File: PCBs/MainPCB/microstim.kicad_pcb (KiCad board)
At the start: 2 copper layers, 124.5 x 79.5 mm, 105 parts, among them J1 Conn_02x08_Odd_Even, J2 Conn_Coaxial, J3 Conn_Coaxial, J6 Screw_Terminal_01x02, J7 Conn_Coaxial, J8 Screw_Terminal_01x02, J9 Conn_Coaxial, SW1 SW_Push, U1 Teensy3.5, U10 AD8276, U11 INA826, U12 DG509ACWE, U13 CC3-0512DF-E, U14 ISO7760, U15 ISO7341C, U16 L78L05_SO8, U17 AD5752, U18 AD7321, U19 AD1582, U2 CC3-0512DF-E, U20 OPA197, U21 AD8276, U22 INA826, U23 DG509ACWE, U3 ISO7760, U4 ISO7341C, U5 L78L05_SO8, U6 AD5752, U7 AD7321, U8 AD1582, U9 OPA197

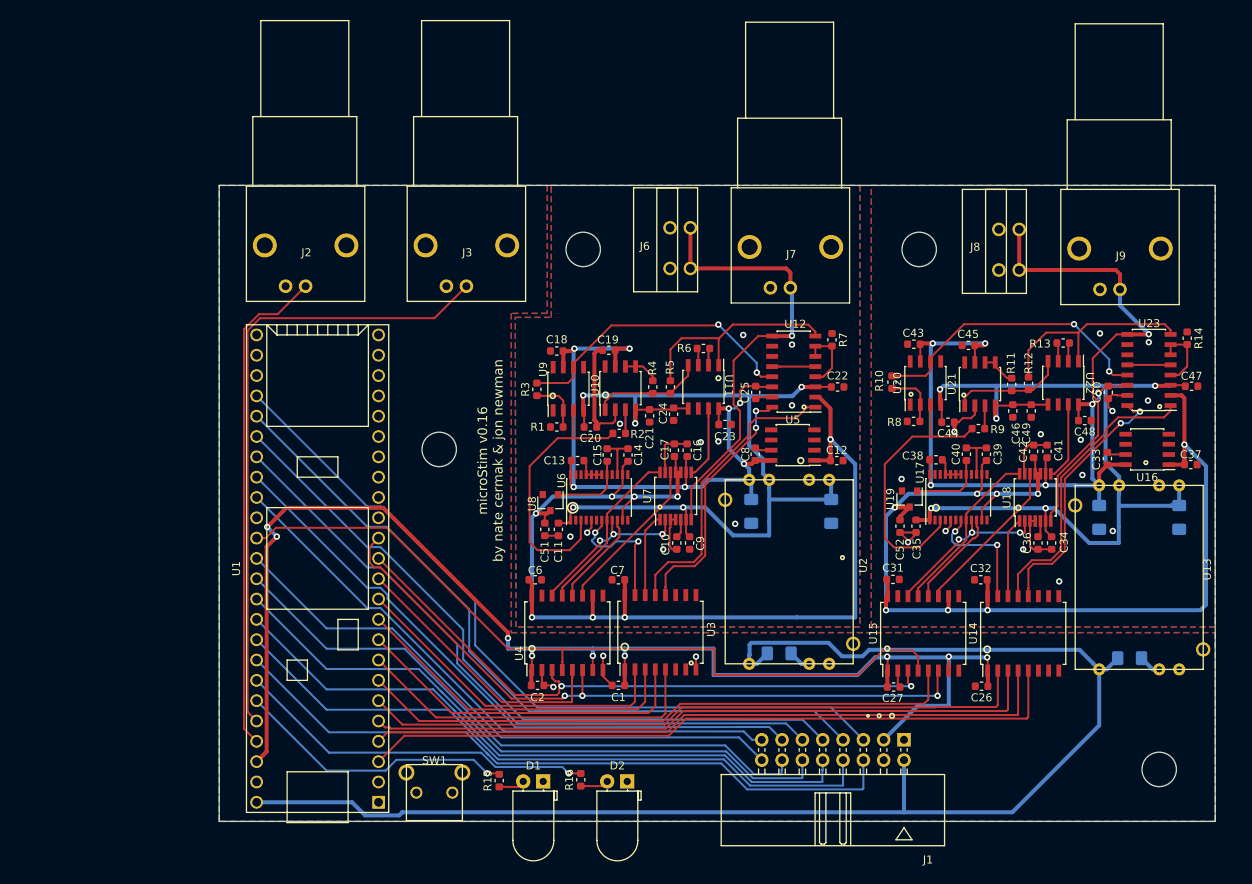
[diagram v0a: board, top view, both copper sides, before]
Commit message: increased board size to 129x79.5 from 124.5x79.5, changed enclosure to something on digikey rather than newark. also added trigger capability to teensy code
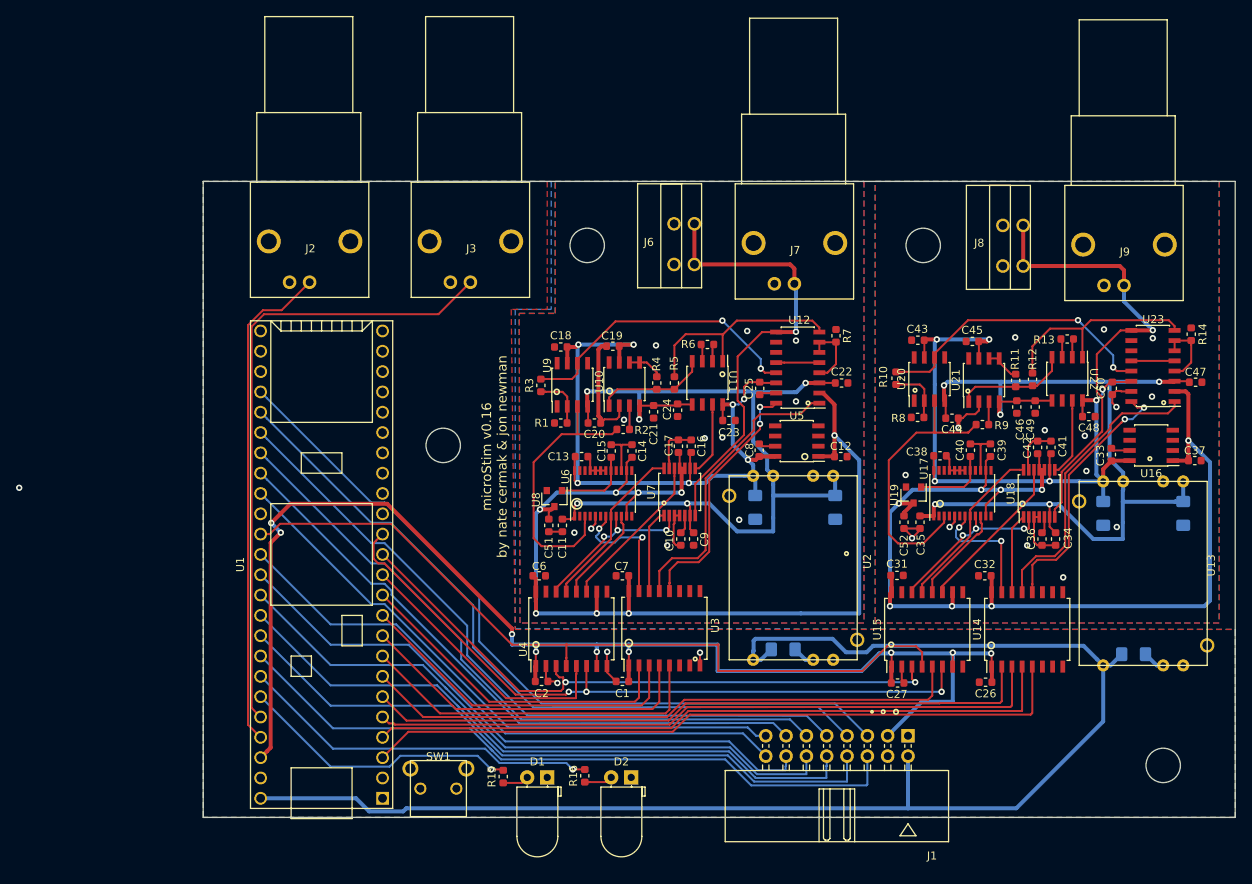
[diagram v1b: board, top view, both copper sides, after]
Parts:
- moved C1 0.71 mm to (132.9, 114.0)
- moved C10 0.71 mm to (140.2, 96.2)
- moved C11 0.71 mm to (125.4, 94.5)
- moved C12 0.71 mm to (160.2, 85.9)
- moved C13 0.71 mm to (127.8, 85.9)
- moved C14 0.71 mm to (134.1, 85.2)
- moved C15 0.71 mm to (131.5, 85.2)
- moved C16 0.71 mm to (141.5, 84.6)
- moved C17 0.71 mm to (139.9, 84.6)
- moved C18 0.71 mm to (125.2, 72.2)
- moved C19 0.71 mm to (131.7, 72.1)
- moved C2 0.71 mm to (122.8, 114.0)
- moved C20 0.71 mm to (129.4, 81.7)
- moved C21 0.71 mm to (136.8, 80.3)
- moved C22 0.71 mm to (160.3, 76.7)
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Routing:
- net GND_1: vias 14 -> 15
- net GND_0: vias 10 -> 11
- net (no net): vias 0 -> 1
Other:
- board size 124.5 x 79.5 mm -> 129 x 79.5 mm

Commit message: boatload of updates via jons suggestions. de-isolated grounds via large resistors+capacitors (to prevent static buildup on animal or issues with large discharges). increased resistor values in voltage output non-inverting amplifier.
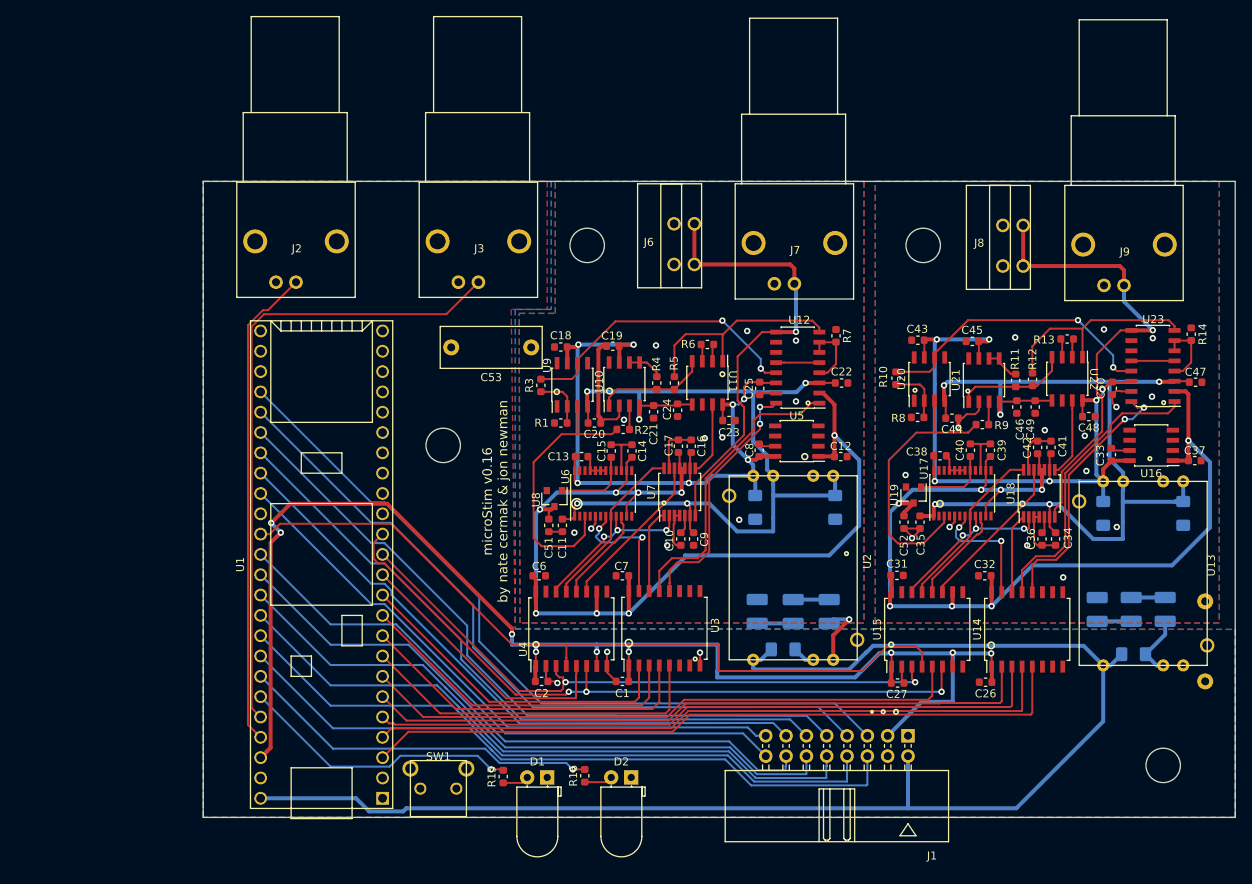
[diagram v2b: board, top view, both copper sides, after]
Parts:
- added C53: C_Small, Capacitor_THT:C_Disc_D12.5mm_W5.0mm_P10.00mm, F.Cu at (121.5, 72.2)
- added C54: C_Small, Capacitor_THT:C_Disc_D12.5mm_W5.0mm_P10.00mm, B.Cu at (205.8, 104.0)
- added R17: R_Small_US, Resistor_SMD:R_1210_3225Metric_Pad1.42x2.65mm_HandSolder, B.Cu at (158.8, 105.3)
- added R18: R_Small_US, Resistor_SMD:R_1210_3225Metric_Pad1.42x2.65mm_HandSolder, B.Cu at (200.8, 105.0)
- added R19: R_Small_US, Resistor_SMD:R_1210_3225Metric_Pad1.42x2.65mm_HandSolder, B.Cu at (154.2, 105.3)
- added R20: R_Small_US, Resistor_SMD:R_1210_3225Metric_Pad1.42x2.65mm_HandSolder, B.Cu at (196.5, 105.0)
- added R21: R_Small_US, Resistor_SMD:R_1210_3225Metric_Pad1.42x2.65mm_HandSolder, B.Cu at (149.8, 105.2)
- added R22: R_Small_US, Resistor_SMD:R_1210_3225Metric_Pad1.42x2.65mm_HandSolder, B.Cu at (192.2, 105.0)
- R1, R8: value 1k -> 10k
- R10, R3: value 500 -> 5k
- moved J2 1.70 mm to (99.5, 59.0)
- moved J3 1.00 mm to (122.3, 59.0)
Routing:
- net GND: track 16.8 -> 30.6 mm, vias 3 -> 4
- net +5V_0: track 139.5 -> 133.1 mm
- net +5V_1: track 133.0 -> 127.6 mm
- net Net-(R19-Pad1): track 0.00 -> 4.51 mm
- net Net-(R17-Pad1): track 0.00 -> 4.50 mm
- net Net-(R20-Pad1): track 0.00 -> 4.26 mm
- net Net-(R18-Pad1): track 0.00 -> 4.25 mm
- net Net-(J2-Pad1): track 62.1 -> 60.4 mm
- net +3V3: track 171.9 -> 173.1 mm
- net VUSB: track 178.1 -> 177.0 mm
- net Net-(J3-Pad1): track 78.9 -> 79.9 mm
- net (no net): vias 1 -> 0

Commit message: changed name to stimjim. added logo-ish thing to board silkscreen. changed ground coupling caps/resistors slightly. renamed a bunch of stuff and replaced most instances of word microstim with stimjim
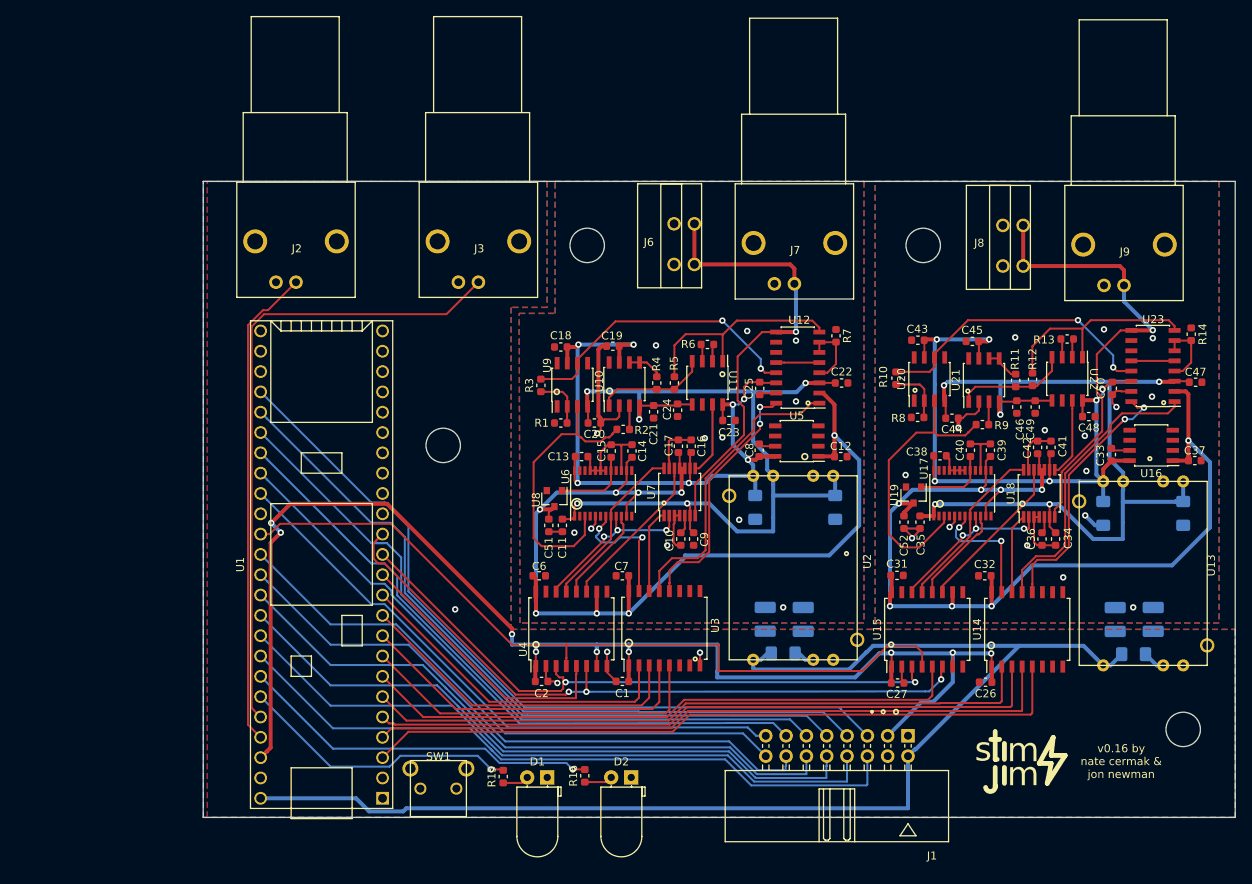
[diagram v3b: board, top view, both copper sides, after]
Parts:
- removed R17, R18, R21, R22: R_Small_US, Resistor_SMD:R_1210_3225Metric_Pad1.42x2.65mm_HandSolder
- C53: value C_Small -> 2.2nF; footprint Capacitor_THT:C_Disc_D12.5mm_W5.0mm_P10.00mm -> Capacitor_SMD:C_1210_3225Metric_Pad1.42x2.65mm_HandSolder; moved to B.Cu
- C54: value C_Small -> 2.2nF; footprint Capacitor_THT:C_Disc_D12.5mm_W5.0mm_P10.00mm -> Capacitor_SMD:C_1210_3225Metric_Pad1.42x2.65mm_HandSolder
- R19, R20: value R_Small_US -> 1M
- moved C53 44.8 mm to (150.8, 106.2), turned to 270 degrees
- moved C54 11.5 mm to (194.5, 106.3)
- moved H4 5.15 mm to (203.0, 120.0)
- moved R20 3.02 mm to (199.2, 106.2), turned to 270 degrees
- moved R19 1.59 mm to (155.5, 106.2), turned to 270 degrees
- moved C3 0.50 mm to (153.0, 110.5)
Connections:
- R19 pad 1: Net-(R19-Pad1) -> GND_0
- R19 pad 2: Net-(R17-Pad1) -> GND
- R20 pad 1: Net-(R20-Pad1) -> GND_1
- R20 pad 2: Net-(R18-Pad1) -> GND
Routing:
- net VUSB: track 177.0 -> 160.7 mm
- net GND: track 30.6 -> 16.8 mm
- net GND_0: track 43.3 -> 49.1 mm, vias 11 -> 12
- net Net-(R19-Pad1): track 4.51 -> 0.00 mm
- net Net-(R17-Pad1): track 4.50 -> 0.00 mm
- net Net-(R20-Pad1): track 4.26 -> 0.00 mm
- net Net-(R18-Pad1): track 4.25 -> 0.00 mm
- net GND_1: track 41.4 -> 44.2 mm, vias 15 -> 16
- net GPIO2: track 88.6 -> 90.8 mm
- net GPIO0: track 96.9 -> 98.4 mm
- net +3V3: track 173.1 -> 171.7 mm
- net GPIO1: track 93.2 -> 94.1 mm
- net MISO: track 88.2 -> 87.3 mm
- net DAC_0: track 35.1 -> 35.8 mm
- net DAC_1: track 35.3 -> 36.0 mm
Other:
- board text added: "m"
- board text added: "s"
- board text added: "v0.16 by nate cermak & jon newman"
- board text removed: "microStim v0.16 by nate cermak & jon newman"
